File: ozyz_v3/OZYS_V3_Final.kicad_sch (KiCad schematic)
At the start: 26 parts, among them CN1 532610571, J1 5037630491, U1 ISO1044BD, U2 STM32G474CETx, U3 MKDV32GCL-STP, X2 MC-306 32.768kHz 6.0pF 20ppm

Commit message: epsilon ready for layout
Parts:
- J1: footprint CON_5037630491 -> (none)
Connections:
- net EEPROM1: no longer names the net of U2.30 (PA8)
- net EEPROM2: no longer names the net of U2.32 (PA10)
- net EEPROM3: no longer names the net of U2.43 (PB6)
- net EEPROM4: no longer names the net of U2.18 (PB2)
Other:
- sheet Receiver1 ports: added none; removed EEPROM_MCU
- sheet Receiver2 ports: added none; removed EEPROM_MCU
- sheet Receiver3 ports: added none; removed EEPROM_MCU
- sheet Receiver4 ports: added none; removed EEPROM_MCU

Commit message: OZYS ready for layout
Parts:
- removed J1: 5037630491, symbol Rocketry_Manual:5037630491
- added C18, C41: 10p, Capacitor_SMD:C_0603_1608Metric_Pad1.08x0.95mm_HandSolder, symbol Device:C
- added C42: 1u, Capacitor_SMD:C_0402_1005Metric, symbol Device:C
- added J_CAN1: 2053380004, Rocketry_Manual:CONN_2053380000-SD_04_MOL, symbol Connector:Conn_01x04_Pin
- added LED5: 19-213/Y2C-CQ2R2L/3T(CY), Rocketry_Easyeda:LED0603-RD-YELLOW, symbol Rocketry_Easyeda:19-213_Y2C-CQ2R2L_3T(CY) (0603 Yellow)
- added Q3: 2N7002, Rocketry_Easyeda:SOT-23-3_L2.9-W1.3-P1.90-LS2.4-BR, symbol Rocketry_Easyeda:2N7002
- added R1: 75R, Resistor_SMD:R_0402_1005Metric, symbol Device:R
- added U5, U6, U7, U8, U9: RH-5015, Rocketry_Easyeda:SMD_RH-5015, symbol Rocketry_Easyeda:RH-5015
- added X1: X322516MLB4SI, Rocketry_Easyeda:OSC-SMD_4P-L3.2-W2.5-BL, symbol Rocketry_Easyeda:X322516MLB4SI
- C1: value 100n -> 10n
- C10: value 100n -> 1u
- C12: value 10u -> 4.7u; footprint Capacitor_SMD:C_0603_1608Metric -> Capacitor_SMD:C_0402_1005Metric
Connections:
- net POWER.VBUS is gone; now on net VBUS: U2.31 (PA9)
- net +3.3V: no longer C5.2, CN1.4, R2.1, R3.1, R38.1, R4.1, R5.1, U1.1 (VCC1)
- net +3V3A: now also C1.1, C11.1, C42.2; no longer C11.2, C12.2, C6.2, C8.2, C9.2, U2.24 (VDD), U2.36 (VDD), U2.48 (VDD)
- net CAN_RXD: now also U2.30 (PA8); no longer U2.42 (PB5)
- net CAN_TXD: now also U2.39 (PA15); no longer U2.27 (PB13)
- net CS: no longer U2.12 (PA4)
- net GND: now also C1.2, C11.2, C12.2, C40.2, C6.2, C8.2, C9.2, C18.1, C41.1, C42.1, Q3.2 (S), U9.1; no longer C1.1, C11.1, C12.1, C40.1, C6.1, C8.1, C9.1
- net LED1: no longer U2.41 (PB4)
- net LED2: no longer U2.39 (PA15)
- net LED3: no longer U2.44 (PB7)
- net LED4: no longer U2.40 (PB3)
- net MKDV32_Clock: now also U2.40 (PB3); no longer U2.13 (PA5)
- net MKDV32_Input: now also U2.42 (PB5); no longer U2.15 (PA7)
- net at BT1.1 (+), U2.1 (VBAT): no longer C1.2
- net at U2.4 (PC15), X2.1: now also C40.1; no longer C40.2
- net at U2.5 (PF0): now also C18.2, X1.3 (OSC2)
- net at U2.6 (PF1): now also C41.2, X1.1 (OSC1)
- net at C3.2, U1.8 (VCC2): now also J_CAN1.1 (Pin_1)
- net at C3.1, U1.7 (GND2): now also J_CAN1.2 (Pin_2)
- net at U1.6 (CANH): now also J_CAN1.3 (Pin_3)
- net at U1.5 (CANL): now also J_CAN1.4 (Pin_4)
- net MKDV32_Ouput renamed MKDV32_Output
- net MKDV32_Output: now also U2.41 (PB4); no longer U2.14 (PA6)
- net POWER.3V3A_SW_EN: no longer names the net of U2.22 (PB10)
- net POWER.BAT_V_M: no longer names the net of U2.28 (PB14)
- net POWER.PS: no longer names the net of U2.46 (PB9)
- net Power/DN renamed USB_DN
- net Power/DP renamed USB_DP
- net Receiver1/DIFFERENTIAL_M: no longer names the net of U2.9 (PA1)
- net Receiver1/DIFFERENTIAL_P: no longer names the net of U2.8 (PA0)
- net Receiver2/DIFFERENTIAL_M: no longer names the net of U2.11 (PA3)
- net Receiver2/DIFFERENTIAL_P: no longer names the net of U2.10 (PA2)
- net Receiver3/DIFFERENTIAL_M: no longer names the net of U2.17 (PB1)
- net Receiver3/DIFFERENTIAL_P: no longer names the net of U2.26 (PB12)
- net Receiver4/DIFFERENTIAL_M: no longer names the net of U2.16 (PB0)
- net Receiver4/DIFFERENTIAL_P: no longer names the net of U2.25 (PB11)
- new net: LED5.1 (C), Q3.3 (D)
- new net: LED5.2 (A), R1.2
- new net +3V3: C12.1, C5.2, C6.1, C8.1, C9.1, CN1.4, R1.1, R2.1, R3.1, R38.1, R4.1, R5.1, U1.1 (VCC1), U2.24 (VDD), U2.36 (VDD), U2.48 (VDD)
- new net 3V3A_SW: U8.1
- new net DM1: U6.1
- new net DP1: U5.1
- new net ONE_WIRE_OUT1: U7.1
- new net STATUS_LED: Q3.1 (G)
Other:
- sheet Receiver1 ports: added ONE_WIRE_OUT; removed none
- sheet Receiver2 ports: added ONE_WIRE_OUT; removed none
- sheet Receiver3 ports: added ONE_WIRE_OUT; removed none
- sheet Receiver4 ports: added ONE_WIRE_OUT; removed none
- note added: "ADC1"
- note added: "ADC2"
- note added: "Any GPIO"
- moved on the sheet: BT1, C12, C13, C39, C4, C40, C6, C8, C9, CN1, R2, R3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

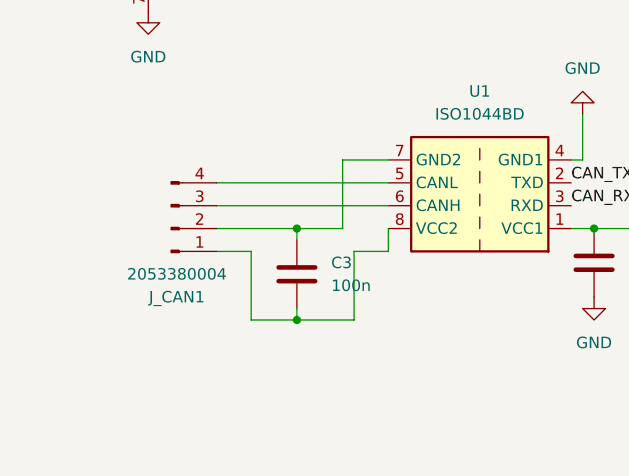
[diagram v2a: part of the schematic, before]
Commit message: update connector placement
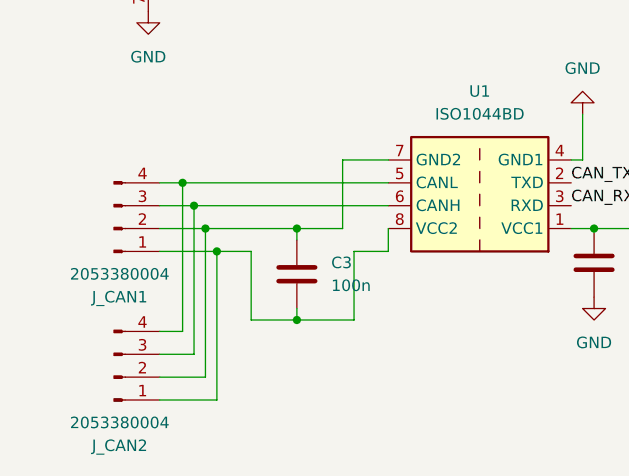
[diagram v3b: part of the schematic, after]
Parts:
- added J_CAN2: 2053380004, Rocketry_Manual:CONN_2053380000-SD_04_MOL, symbol Connector:Conn_01x04_Pin
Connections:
- net at J_CAN1.4 (Pin_4), U1.5 (CANL): now also J_CAN2.4 (Pin_4)
- net at J_CAN1.3 (Pin_3), U1.6 (CANH): now also J_CAN2.3 (Pin_3)
- net at C3.1, J_CAN1.2 (Pin_2), U1.7 (GND2): now also J_CAN2.2 (Pin_2)
- net at C3.2, J_CAN1.1 (Pin_1), U1.8 (VCC2): now also J_CAN2.1 (Pin_1)
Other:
- moved on the sheet: J_CAN1
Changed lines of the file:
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@@
 	)
 	(junction
+		(at 33.02 168.91)
+		(diameter 0)
+		(color 0 0 0 0)
+	)
+	(junction
 		(at 116.84 130.81)
 		(diameter 0)
@@
 	)
 	(junction
+		(at 31.75 166.37)
+		(diameter 0)
+		(color 0 0 0 0)
+	)
+	(junction
 		(at 140.97 35.56)
 		(diameter 0)
@@
 	)
 	(junction
+		(at 35.56 173.99)
+		(diameter 0)
+		(color 0 0 0 0)
+	)
+	(junction
 		(at 229.87 127)
 		(diameter 0)
@@
 	)
 	(junction
+		(at 34.29 171.45)
+		(diameter 0)
+		(color 0 0 0 0)
+	)
+	(junction
 		(at 118.11 44.45)
 		(diameter 0)
@@
 	(wire
 		(pts
+			(xy 33.02 185.42) (xy 33.02 168.91)
+		)
+		(stroke
+			(width 0)
+			(type default)
+		)
+	)
+	(wire
+		(pts
 			(xy 233.68 142.24) (xy 233.68 144.78)
 		)
@@
 	(wire
 		(pts
+			(xy 31.75 182.88) (xy 31.75 166.37)
+		)
+		(stroke
+			(width 0)
+			(type default)
+		)
+	)
+	(wire
+		(pts
 			(xy 44.45 134.62) (xy 34.29 134.62)
 		)
@@
 	(wire
 		(pts
+			(xy 35.56 173.99) (xy 29.21 173.99)
+		)
+		(stroke
+			(width 0)
+			(type default)
+		)
+	)
+	(wire
+		(pts
 			(xy 120.65 35.56) (xy 127 35.56)
 		)
@@
 	(wire
 		(pts
+			(xy 31.75 166.37) (xy 54.61 166.37)
+		)
+		(stroke
+			(width 0)
+			(type default)
+		)
+	)
+	(wire
+		(pts
+			(xy 29.21 187.96) (xy 34.29 187.96)
+		)
+		(stroke
+			(width 0)
+			(type default)
+		)
+	)
+	(wire
+		(pts
 			(xy 234.95 134.62) (xy 233.68 134.62)
 		)
@@
 	(wire
 		(pts
-			(xy 35.56 171.45) (xy 44.45 171.45)
+			(xy 29.21 171.45) (xy 34.29 171.45)
 		)
 		(stroke
@@
 	(wire
 		(pts
+			(xy 33.02 168.91) (xy 54.61 168.91)
+		)
+		(stroke
+			(width 0)
+			(type default)
+		)
+	)
+	(wire
+		(pts
 			(xy 66.04 34.29) (xy 74.93 34.29)
 		)
@@
 	(wire
 		(pts
+			(xy 29.21 185.42) (xy 33.02 185.42)
+		)
+		(stroke
+			(width 0)
+			(type default)
+		)
+	)
+	(wire
+		(pts
 			(xy 118.11 22.86) (xy 118.11 44.45)
 		)
@@
 	(wire
 		(pts
+			(xy 29.21 182.88) (xy 31.75 182.88)
+		)
+		(stroke
+			(width 0)
+			(type default)
+		)
+	)
+	(wire
+		(pts
 			(xy 33.02 96.52) (xy 33.02 97.79)
 		)
@@
 	(wire
 		(pts
+			(xy 29.21 190.5) (xy 35.56 190.5)
+		)
+		(stroke
+			(width 0)
+			(type default)
+		)
+	)
+	(wire
+		(pts
 			(xy 34.29 139.7) (xy 44.45 139.7)
 		)
@@
 	(wire
 		(pts
+			(xy 34.29 171.45) (xy 44.45 171.45)
+		)
+		(stroke
+			(width 0)
+			(type default)
+		)
+	)
+	(wire
+		(pts
 			(xy 100.33 22.86) (xy 102.87 22.86)
 		)
@@
 	(wire
 		(pts
-			(xy 35.56 168.91) (xy 54.61 168.91)
+			(xy 29.21 168.91) (xy 33.02 168.91)
 		)
 		(stroke
@@
 	(wire
 		(pts
-			(xy 35.56 166.37) (xy 54.61 166.37)
+			(xy 29.21 166.37) (xy 31.75 166.37)
 		)
 		(stroke
@@
 	(wire
 		(pts
+			(xy 34.29 187.96) (xy 34.29 171.45)
+		)
+		(stroke
+			(width 0)
+			(type default)
+		)
+	)
+	(wire
+		(pts
 			(xy 220.98 132.08) (xy 234.95 132.08)
 		)
@@
 	(wire
 		(pts
+			(xy 35.56 190.5) (xy 35.56 173.99)
+		)
+		(stroke
+			(width 0)
+			(type default)
+		)
+	)
+	(wire
+		(pts
 			(xy 140.97 22.86) (xy 154.94 22.86)
 		)
@@
 	(symbol
 		(lib_id "Connector:Conn_01x04_Pin")
-		(at 30.48 171.45 0)
+		(at 24.13 171.45 0)
 		(mirror x)
 		(unit 1)
@@
 		(dnp no)
 		(property "Reference" "J_CAN1"
-			(at 31.115 179.07 0)
+			(at 24.765 179.07 0)
 			(effects
 				(font
@@
 		)
 		(property "Value" "2053380004"
-			(at 31.115 176.53 0)
+			(at 24.765 176.53 0)
 			(effects
 				(font
@@
 		)
 		(property "Footprint" "Rocketry_Manual:CONN_2053380000-SD_04_MOL"
-			(at 30.48 171.45 0)
+			(at 24.13 171.45 0)
 			(effects
 				(font
@@
 		)
 		(property "Datasheet" "~"
-			(at 30.48 171.45 0)
+			(at 24.13 171.45 0)
 			(effects
 				(font
@@
 		)
 		(property "Description" "Generic connector, single row, 01x04, script generated"
-			(at 30.48 171.45 0)
+			(at 24.13 171.45 0)
 			(effects
 				(font
@@
 					(unit 1)
 				)
+			)
+		)
+	)
+	(symbol
+		(lib_id "Connector:Conn_01x04_Pin")
+		(at 24.13 187.96 0)
+		(mirror x)
+		(unit 1)
+		(exclude_from_sim no)
+		(in_bom yes)
+		(on_board yes)
+		(dnp no)
+		(property "Reference" "J_CAN2"
+			(at 24.765 195.58 0)
+			(effects
+				(font
+					(size 1.27 1.27)
+				)
+			)
+		)
+		(property "Value" "2053380004"
+			(at 24.765 193.04 0)
+			(effects
+				(font
+					(size 1.27 1.27)
+				)
+			)
+		)
+		(property "Footprint" "Rocketry_Manual:CONN_2053380000-SD_04_MOL"
+			(at 24.13 187.96 0)
+			(effects
+				(font
+					(size 1.27 1.27)
+				)
+				(hide yes)
+			)
+		)
+		(property "Datasheet" "~"
+			(at 24.13 187.96 0)
+			(effects
+				(font
+					(size 1.27 1.27)
+				)
+				(hide yes)
+			)
+		)
+		(property "Description" "Generic connector, single row, 01x04, script generated"
+			(at 24.13 187.96 0)
+			(effects
+				(font
+					(size 1.27 1.27)
+				)
+				(hide yes)
+			)
+		)
+		(pin "2"
+		)
+		(pin "3"
+		)
+		(pin "4"
+		)
+		(pin "1"
+		)
+		(instances
+			(project "OZYS_V3_Final"
+				(path "/2ecddb92-e766-42eb-adbc-b6d17a65e8ea"
+					(reference "J_CAN2")
+					(unit 1)
+				)

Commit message: Saving Rough Iteration of Ozys V3
-STM Pins to be configured with current layout
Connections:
- net 3V3A_SW_EN: now also U2.27 (PB13)
- net BAT_V_M: now also U2.18 (PB2)
- net CS: now also U2.46 (PB9)
- net DM1: now also U2.9 (PA1)
- net DM2: now also U2.16 (PB0)
- net DM3: now also U2.17 (PB1)
- net DM4: now also U2.11 (PA3)
- net DP1: now also U2.8 (PA0)
- net DP2: now also U2.25 (PB11)
- net DP3: now also U2.26 (PB12)
- net DP4: now also U2.10 (PA2)
- net ONE_WIRE_OUT1: now also U2.12 (PA4)
- net ONE_WIRE_OUT2: now also U2.14 (PA6)
- net ONE_WIRE_OUT3: now also U2.13 (PA5)
- net ONE_WIRE_OUT4: now also U2.29 (PB15)
- net PS: now also U2.15 (PA7)
- net STATUS_LED: now also U2.28 (PB14)
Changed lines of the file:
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@@
-	(wire
-		(pts
-			(xy 40.64 68.58) (xy 97.79 68.58)
-		)
-		(stroke
-			(width 0)
-			(type default)
-		)
-	)
 	(wire
 		(pts
@@
 	(wire
 		(pts
+			(xy 38.1 68.58) (xy 97.79 68.58)
+		)
+		(stroke
+			(width 0)
+			(type default)
+		)
+	)
+	(wire
+		(pts
 			(xy 120.65 35.56) (xy 127 35.56)
 		)
@@
 	(wire
 		(pts
+			(xy 96.52 96.52) (xy 97.79 96.52)
+		)
+		(stroke
+			(width 0)
+			(type default)
+		)
+	)
+	(wire
+		(pts
 			(xy 29.21 187.96) (xy 34.29 187.96)
 		)
@@
 	(wire
 		(pts
-			(xy 40.64 54.61) (xy 33.02 54.61)
+			(xy 38.1 54.61) (xy 33.02 54.61)
 		)
 		(stroke
@@
 	(wire
 		(pts
+			(xy 96.52 91.44) (xy 97.79 91.44)
+		)
+		(stroke
+			(width 0)
+			(type default)
+		)
+	)
+	(wire
+		(pts
 			(xy 115.57 129.54) (xy 115.57 130.81)
 		)
@@
 	(wire
 		(pts
-			(xy 40.64 54.61) (xy 40.64 68.58)
+			(xy 38.1 54.61) (xy 38.1 68.58)
 		)
 		(stroke
@@
 		(pts
 			(xy 54.61 173.99) (xy 54.61 171.45)
+		)
+		(stroke
+			(width 0)
+			(type default)
+		)
+	)
+	(wire
+		(pts
+			(xy 96.52 93.98) (xy 97.79 93.98)
 		)
 		(stroke
@@
 	)
 	(label "CS"
-		(at 157.48 78.74 0)
-		(effects
-			(font
-				(size 1.27 1.27)
-			)
-			(justify left bottom)
+		(at 97.79 106.68 180)
+		(effects
+			(font
+				(size 1.27 1.27)
+			)
+			(justify right bottom)
 		)
 	)
@@
 	)
 	(label "DM4"
-		(at 173.99 86.36 0)
+		(at 133.35 63.5 0)
 		(effects
 			(font
@@
 	)
 	(label "DM1"
-		(at 173.99 71.12 0)
+		(at 133.35 58.42 0)
 		(effects
 			(font
@@
 	)
 	(label "MKDV32_Input"
-		(at 97.79 96.52 180)
+		(at 96.52 96.52 180)
 		(effects
 			(font
@@
 	)
 	(label "DP2"
-		(at 173.99 73.66 0)
-		(effects
-			(font
-				(size 1.27 1.27)
-			)
-			(justify left bottom)
+		(at 97.79 111.76 180)
+		(effects
+			(font
+				(size 1.27 1.27)
+			)
+			(justify right bottom)
 		)
 	)
 	(label "DP1"
-		(at 173.99 68.58 0)
+		(at 133.35 55.88 0)
 		(effects
 			(font
@@
 	)
 	(label "ONE_WIRE_OUT4"
-		(at 189.23 76.2 0)
-		(effects
-			(font
-				(size 1.27 1.27)
-			)
-			(justify left bottom)
+		(at 97.79 121.92 180)
+		(effects
+			(font
+				(size 1.27 1.27)
+			)
+			(justify right bottom)
 		)
 	)
 	(label "DP3"
-		(at 173.99 78.74 0)
-		(effects
-			(font
-				(size 1.27 1.27)
-			)
-			(justify left bottom)
+		(at 97.79 114.3 180)
+		(effects
+			(font
+				(size 1.27 1.27)
+			)
+			(justify right bottom)
 		)
 	)
 	(label "DP4"
-		(at 173.99 83.82 0)
+		(at 133.35 60.96 0)
 		(effects
 			(font
@@
 	)
 	(label "ONE_WIRE_OUT1"
-		(at 189.23 68.58 0)
+		(at 133.35 66.04 0)
 		(effects
 			(font
@@
 	)
 	(label "3V3A_SW_EN"
-		(at 157.48 83.82 0)
-		(effects
-			(font
-				(size 1.27 1.27)
-			)
-			(justify left bottom)
+		(at 97.79 116.84 180)
+		(effects
+			(font
+				(size 1.27 1.27)
+			)
+			(justify right bottom)
 		)
 	)
@@
 	)
 	(label "ONE_WIRE_OUT3"
-		(at 189.23 73.66 0)
+		(at 133.35 68.58 0)
 		(effects
 			(font
@@
 	)
 	(label "DM3"
-		(at 173.99 81.28 0)
-		(effects
-			(font
-				(size 1.27 1.27)
-			)
-			(justify left bottom)
+		(at 97.79 86.36 180)
+		(effects
+			(font
+				(size 1.27 1.27)
+			)
+			(justify right bottom)
 		)
 	)
@@
 	)
 	(label "PS"
-		(at 157.48 81.28 0)
+		(at 133.35 73.66 0)
 		(effects
 			(font
@@
 	)
 	(label "MKDV32_Clock"
-		(at 97.79 91.44 180)
+		(at 96.52 91.44 180)
 		(effects
 			(font
@@
 	)
 	(label "ONE_WIRE_OUT2"
-		(at 189.23 71.12 0)
+		(at 133.35 71.12 0)
 		(effects
 			(font
@@
 	)
 	(label "BAT_V_M"
-		(at 189.23 78.74 0)
-		(effects
-			(font
-				(size 1.27 1.27)
-			)
-			(justify left bottom)
+		(at 97.79 88.9 180)
+		(effects
+			(font
+				(size 1.27 1.27)
+			)
+			(justify right bottom)
 		)
 	)
 	(label "STATUS_LED"
-		(at 157.48 86.36 0)
-		(effects
-			(font
-				(size 1.27 1.27)
-			)
-			(justify left bottom)
+		(at 97.79 119.38 180)
+		(effects
+			(font
+				(size 1.27 1.27)
+			)
+			(justify right bottom)
 		)
 	)
 	(label "DM2"
-		(at 173.99 76.2 0)
-		(effects
-			(font
-				(size 1.27 1.27)
-			)
-			(justify left bottom)
+		(at 97.79 83.82 180)
+		(effects
+			(font
+				(size 1.27 1.27)
+			)
+			(justify right bottom)
 		)
 	)
@@
 	)
 	(label "MKDV32_Output"
-		(at 97.79 93.98 180)
+		(at 96.52 93.98 180)
 		(effects
 			(font
@@
 		(on_board yes)
 		(dnp no)
-		(fields_autoplaced yes)
 		(property "Reference" "U2"
 			(at 120.3041 129.54 0)

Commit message: Fixed LEDs
- Just need to clean it up then add pours and GND vias
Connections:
- net +3.3V is gone; now on net +3V3: C13.2, U3.8 (VDD)
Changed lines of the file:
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@@
 	(wire
 		(pts
+			(xy 222.25 127) (xy 229.87 127)
+		)
+		(stroke
+			(width 0)
+			(type default)
+		)
+	)
+	(wire
+		(pts
 			(xy 238.76 142.24) (xy 233.68 142.24)
 		)
@@
 	(wire
 		(pts
+			(xy 222.25 123.19) (xy 222.25 127)
+		)
+		(stroke
+			(width 0)
+			(type default)
+		)
+	)
+	(wire
+		(pts
 			(xy 118.11 129.54) (xy 118.11 130.81)
 		)
@@
 	(wire
 		(pts
-			(xy 229.87 127) (xy 226.06 127)
-		)
-		(stroke
-			(width 0)
-			(type default)
-		)
-	)
-	(wire
-		(pts
 			(xy 95.25 34.29) (xy 88.9 34.29)
 		)
@@
 	)
 	(symbol
+		(lib_id "power:+3.3V")
+		(at 222.25 123.19 0)
+		(unit 1)
+		(exclude_from_sim no)
+		(in_bom yes)
+		(on_board yes)
+		(dnp no)
+		(property "Reference" "#PWR013"
+			(at 222.25 127 0)
+			(effects
+				(font
+					(size 1.27 1.27)
+				)
+				(hide yes)
+			)
+		)
+		(property "Value" "+3V3"
+			(at 222.2501 119.38 90)
+			(effects
+				(font
+					(size 1.27 1.27)
+				)
+				(justify left)
+			)
+		)
+		(property "Footprint" ""
+			(at 222.25 123.19 0)
+			(effects
+				(font
+					(size 1.27 1.27)
+				)
+				(hide yes)
+			)
+		)
+		(property "Datasheet" ""
+			(at 222.25 123.19 0)
+			(effects
+				(font
+					(size 1.27 1.27)
+				)
+				(hide yes)
+			)
+		)
+		(property "Description" "Power symbol creates a global label with name \"+3.3V\""
+			(at 222.25 123.19 0)
+			(effects
+				(font
+					(size 1.27 1.27)
+				)
+				(hide yes)
+			)
+		)
+		(pin "1"
+		)
+		(instances
+			(project "OZYS_V3_Final"
+				(path "/2ecddb92-e766-42eb-adbc-b6d17a65e8ea"
+					(reference "#PWR013")
+					(unit 1)
+				)
+			)
+		)
+	)
+	(symbol
 		(lib_id "power:GND")
 		(at 116.84 130.81 0)
@@
 					(unit 1)
 				)
-			)
-		)
-	)
-	(symbol
-		(lib_id "power:+3.3V")
-		(at 226.06 127 90)
-		(mirror x)
-		(unit 1)
-		(exclude_from_sim no)
-		(in_bom yes)
-		(on_board yes)
-		(dnp no)
-		(fields_autoplaced yes)
-		(property "Reference" "#PWR013"
-			(at 229.87 127 0)
-			(effects
-				(font
-					(size 1.27 1.27)
-				)
-				(hide yes)
-			)
-		)
-		(property "Value" "+3.3V"
-			(at 222.25 126.9999 90)
-			(effects
-				(font
-					(size 1.27 1.27)
-				)
-				(justify left)
-			)
-		)
-		(property "Footprint" ""
-			(at 226.06 127 0)
-			(effects
-				(font
-					(size 1.27 1.27)
-				)
-				(hide yes)
-			)
-		)
-		(property "Datasheet" ""
-			(at 226.06 127 0)
-			(effects
-				(font
-					(size 1.27 1.27)
-				)
-				(hide yes)
-			)
-		)
-		(property "Description" "Power symbol creates a global label with name \"+3.3V\""
-			(at 226.06 127 0)
-			(effects
-				(font
-					(size 1.27 1.27)
-				)
-				(hide yes)
-			)
-		)
-		(pin "1"
-		)
-		(instances
-			(project "OZYS_V3_Final"
-				(path "/2ecddb92-e766-42eb-adbc-b6d17a65e8ea"
-					(reference "#PWR013")
-					(unit 1)
-				)

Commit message: fixed connections and playing with pours
as summary describes
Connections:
- net LED1: now also U2.2 (PC13)
- net LED2: now also U2.32 (PA10)
- net LED3: now also U2.44 (PB7)
- net LED4: now also U2.43 (PB6)
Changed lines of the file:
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@@
 	)
 	(label "LED4"
-		(at 157.48 76.2 0)
-		(effects
-			(font
-				(size 1.27 1.27)
-			)
-			(justify left bottom)
+		(at 97.79 99.06 180)
+		(effects
+			(font
+				(size 1.27 1.27)
+			)
+			(justify right bottom)
 		)
 	)
@@
 	)
 	(label "LED2"
-		(at 157.48 71.12 0)
+		(at 133.35 81.28 0)
 		(effects
 			(font
@@
 	)
 	(label "LED1"
-		(at 157.48 68.58 0)
-		(effects
-			(font
-				(size 1.27 1.27)
-			)
-			(justify left bottom)
+		(at 97.79 73.66 180)
+		(effects
+			(font
+				(size 1.27 1.27)
+			)
+			(justify right bottom)
 		)
 	)
@@
 	)
 	(label "LED3"
-		(at 157.48 73.66 0)
-		(effects
-			(font
-				(size 1.27 1.27)
-			)
-			(justify left bottom)
-		)
-	)
+		(at 97.79 101.6 180)
+		(effects
+			(font
+				(size 1.27 1.27)
+			)
+			(justify right bottom)
+		)
+	)
